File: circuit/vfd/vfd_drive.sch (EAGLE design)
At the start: 51 parts, among them J1 ZX62R-AB-5P, J2 DC_JACK_2DC0005D100, J8 FSM-21045-8, Q1 FA-238V, SW1 SKRPACE010, SW2 SKRPACE010, U1 PIC18F14K50-I, U2 MAX6921AWI+, U3 NJW4131, U4 DS3231M, U5 ADP3338AKCZ-3.3, U6 PSF-A85, U9 BME280

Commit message: [add]add all
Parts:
- removed J8: FSM-21045-8, taki-library:FSM-21045-8
- removed Q1: FA-238V, taki-library:FA-238V
- added C12: 0.1uF, taki-library:C-EUC0603
- added C17: 47pF, taki-library:C-EUC0603
- added J3: FSM-21045-10, taki-library:FSM-21045-10
- added J5: PSM-210223-10, taki-library:PSM-210223-10
- added LED1: RX, taki-library:LEDCHIPLED_0603
- added LED2: TX, taki-library:LEDCHIPLED_0603
- added LED4: VBUS, taki-library:LEDCHIPLED_0603
- added Q2, Q3: MMSS8050-L, taki-library:MMSS8050-L
- added R12, R13, R14: 1k, taki-library:R-EU_R0603
- added R15: 4.7k, taki-library:R-EU_R0603
- added R16, R19, R22, R23, R24: 10k, taki-library:R-EU_R0603
- added R17, R18: 27, taki-library:R-EU_R0603
- C16: value 0.1uF -> 47pF
- C3, C4: value 15pF -> 1uF
- J2: value DC_JACK_2DC0005D100 -> 2DC-0415D200; device taki-library:DC_JACK_2DC0005D100 -> taki-library:2DC-0415D200
- U1: value PIC18F14K50-I -> FT231XS; device taki-library:PIC18F14K50-I -> taki-library:FT231XS
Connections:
- removed net D_N: J1.D-, U1.RA1/D-
- removed net D_P: J1.D+, U1.RA0/D+
- removed net EN: C7.1, R3.1, R4.2
- removed net N$39: U1.VUSB
- removed net N$44: C3.1, Q1.1, U1.RA5/OSC1
- removed net N$45: C4.1, Q1.3, U1.RA4/OSC2
- removed net VBIAS: C1.1, DIS1.VBIAS
- new net D2_N: R17.2, U1.USBDM
- new net D2_P: R18.2, U1.USBDP
- new net DTR: Q3.E, R19.2, U1.!DTR
- new net D_N1: C16.1, J1.D-, R17.1
- new net D_P1: C17.1, J1.D+, R18.1
- new net N$14: R15.1, R16.2, U1.CBUS0
- new net N$15: Q2.B, R19.1
- new net N$16: Q3.B, R22.1
- new net N$17: R10.2
- new net N$18: J5.6, U2.VFBLANK
- new net N$19: R23.2, U6.GPIO15
- new net N$21: R24.1, U6.EN
- new net N$7: LED1.C, U1.CBUS1
- new net RESET: C7.1, Q2.C, R3.1, R4.2
- new net RTS: Q2.E, R22.2, U1.!RTS
- new net RXD: U1.RXD, U6.TX
- new net TXD: U1.TXD, U6.RX
- net +3V3: now also C12.1, C4.1, R12.2, R13.2, R24.2, U1.!RESET, U1.3V3OUT, U1.VCC, U1.VCCIO, U6.3V3; no longer C16.1, U1.VDD
- net +5V: now also C1.1, C3.1, DIS1.VBIAS, J5.1
- net GND: now also C12.2, C17.2, LED4.C, R16.1, R23.1, U1.GND@16, U1.GND@6, U2.GND, U6.GND1, U6.GND2; no longer Q1.2, Q1.4, U1.VSS
- net IO0: now also Q3.C
- net N$10: now also LED2.A, R13.1; no longer J8.5, U1.RC6/AN8
- net N$11: now also LED4.A, R14.1; no longer J8.4, U1.RC7/AN9
- net N$2: now also J5.2
- net N$3: now also J5.3
- net N$4: now also J5.4
- net N$5: now also J5.5
- net N$8: now also LED2.C, U1.CBUS2; no longer J8.7, U1.RC4/P1B
- net N$9: now also LED1.A, R12.1; no longer J8.6, U1.RC3/AN7
- net SCL: no longer U1.RB6
- net SDA: no longer U1.RB4/AN10
- net VBUS: now also R14.2, R15.2; no longer R10.2
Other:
- moved on the sheet: C15, C16, C3, C4, J1, J2

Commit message: [update]update from thinkpad
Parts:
- removed LED3: VBUS, taki-library:LEDCHIPLED_0603
- removed R10: 1k, taki-library:R-EU_R0603
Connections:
- removed net N$13: LED3.A, R10.1
- removed net N$17: R10.2
- net GND: no longer LED3.C
- net IO0: now also U6.GPIO0
- net RESET: now also U6.RESET
- net SDA: now also U6.GPIO14, U6.GPIO2
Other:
- moved on the sheet: R24
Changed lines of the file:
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@@
 </classes>
 <parts>
-<part name="SUPPLY1" library="taki-library" deviceset="GND" device=""/>
 <part name="R3" library="taki-library" deviceset="R-EU_" device="R0603" value="10k"/>
 <part name="C7" library="taki-library" deviceset="C-EU" device="C0603" value="1000pF "/>
@@
 <part name="GND8" library="taki-library" deviceset="GND" device=""/>
 <part name="+3V9" library="taki-library" deviceset="+3V3" device=""/>
-<part name="R10" library="taki-library" deviceset="R-EU_" device="R0603" value="1k"/>
-<part name="SUPPLY10" library="taki-library" deviceset="GND" device=""/>
 <part name="J1" library="taki-library" deviceset="ZX62" device="" technology="R-AB-5P"/>
-<part name="LED3" library="taki-library" deviceset="LED" device="CHIPLED_0603" value="VBUS"/>
 <part name="SW1" library="taki-library" deviceset="SKRPACE010" device=""/>
 <part name="SW2" library="taki-library" deviceset="SKRPACE010" device=""/>
@@
 </plain>
 <instances>
-<instance part="SUPPLY1" gate="GND" x="-154.94" y="88.9" smashed="yes">
-<attribute name="VALUE" x="-156.845" y="85.725" size="1.778" layer="96"/>
-</instance>
 <instance part="R3" gate="G$1" x="-116.84" y="-5.08" smashed="yes" rot="R90">
 <attribute name="NAME" x="-118.3386" y="-8.89" size="1.778" layer="95" rot="R90"/>
@@
 <attribute name="VALUE" x="-119.38" y="-40.64" size="1.778" layer="96" rot="R90"/>
 </instance>
-<instance part="R10" gate="G$1" x="-147.32" y="93.98" smashed="yes" rot="R90">
-<attribute name="NAME" x="-148.8186" y="90.17" size="1.778" layer="95" rot="R90"/>
-<attribute name="VALUE" x="-144.018" y="90.17" size="1.778" layer="96" rot="R90"/>
-</instance>
-<instance part="SUPPLY10" gate="GND" x="-147.32" y="73.66" smashed="yes">
-<attribute name="VALUE" x="-149.225" y="70.485" size="1.778" layer="96"/>
-</instance>
 <instance part="J1" gate="G$1" x="-266.7" y="-215.9" smashed="yes">
 <attribute name="NAME" x="-275.844" y="-207.772" size="1.778" layer="95"/>
 <attribute name="VALUE" x="-275.59" y="-231.14" size="1.778" layer="96"/>
 </instance>
-<instance part="LED3" gate="G$1" x="-147.32" y="83.82" smashed="yes">
-<attribute name="NAME" x="-143.764" y="79.248" size="1.778" layer="95" rot="R90"/>
-<attribute name="VALUE" x="-141.605" y="79.248" size="1.778" layer="96" rot="R90"/>
-</instance>
 <instance part="SW1" gate="G$1" x="-142.24" y="-12.7" smashed="yes" rot="R270">
 <attribute name="NAME" x="-144.78" y="-6.35" size="1.778" layer="95"/>
@@
 <attribute name="VALUE" x="-207.645" y="-3.175" size="1.778" layer="96"/>
 </instance>
-<instance part="R24" gate="G$1" x="-271.78" y="17.78" smashed="yes" rot="R90">
-<attribute name="NAME" x="-273.2786" y="13.97" size="1.778" layer="95" rot="R90"/>
-<attribute name="VALUE" x="-268.478" y="13.97" size="1.778" layer="96" rot="R90"/>
-</instance>
-<instance part="+3V5" gate="G$1" x="-271.78" y="27.94" smashed="yes">
-<attribute name="VALUE" x="-274.32" y="22.86" size="1.778" layer="96" rot="R90"/>
+<instance part="R24" gate="G$1" x="-271.78" y="22.86" smashed="yes" rot="R90">
+<attribute name="NAME" x="-273.2786" y="19.05" size="1.778" layer="95" rot="R90"/>
+<attribute name="VALUE" x="-268.478" y="19.05" size="1.778" layer="96" rot="R90"/>
+</instance>
+<instance part="+3V5" gate="G$1" x="-271.78" y="33.02" smashed="yes">
+<attribute name="VALUE" x="-274.32" y="27.94" size="1.778" layer="96" rot="R90"/>
 </instance>
 <instance part="+3V6" gate="G$1" x="-185.42" y="22.86" smashed="yes">
@@
 </net>
 <net name="GND" class="0">
-<segment>
-<pinref part="SUPPLY1" gate="GND" pin="GND"/>
-<wire x1="-154.94" y1="101.6" x2="-154.94" y2="91.44" width="0.1524" layer="91"/>
-</segment>
 <segment>
 <pinref part="J1" gate="G$1" pin="GND"/>
@@
 <pinref part="SW2" gate="G$1" pin="P"/>
 <pinref part="SW2" gate="G$1" pin="P1"/>
-</segment>
-<segment>
-<wire x1="-147.32" y1="78.74" x2="-147.32" y2="76.2" width="0.1524" layer="91"/>
-<pinref part="SUPPLY10" gate="GND" pin="GND"/>
-<pinref part="LED3" gate="G$1" pin="C"/>
 </segment>
 <segment>
@@
 <pinref part="R24" gate="G$1" pin="2"/>
 <pinref part="+3V5" gate="G$1" pin="+3V3"/>
-<wire x1="-271.78" y1="22.86" x2="-271.78" y2="25.4" width="0.1524" layer="91"/>
+<wire x1="-271.78" y1="27.94" x2="-271.78" y2="30.48" width="0.1524" layer="91"/>
 </segment>
 <segment>
@@
 <pinref part="Q2" gate="G$1" pin="C"/>
 </segment>
+<segment>
+<wire x1="-215.9" y1="15.24" x2="-205.74" y2="15.24" width="0.1524" layer="91"/>
+<pinref part="U6" gate="G$1" pin="RESET"/>
+<label x="-208.28" y="15.24" size="1.778" layer="95"/>
+</segment>
 </net>
 <net name="IO0" class="0">
@@
 <wire x1="-218.44" y1="-307.34" x2="-215.9" y2="-307.34" width="0.1524" layer="91"/>
 <pinref part="Q3" gate="G$1" pin="C"/>
+</segment>
+<segment>
+<wire x1="-246.38" y1="-25.4" x2="-246.38" y2="-17.78" width="0.1524" layer="91"/>
+<pinref part="U6" gate="G$1" pin="GPIO0"/>
+<label x="-246.38" y="-25.4" size="1.778" layer="95" rot="R90"/>
 </segment>
 </net>
@@
 </segment>
 </net>
-<net name="N$13" class="0">
-<segment>
-<pinref part="R10" gate="G$1" pin="1"/>
-<wire x1="-147.32" y1="86.36" x2="-147.32" y2="88.9" width="0.1524" layer="91"/>
-<pinref part="LED3" gate="G$1" pin="A"/>
-</segment>
-</net>
 <net name="VBATT" class="0">
 <segment>
@@
 <wire x1="-58.42" y1="45.72" x2="-58.42" y2="50.8" width="0.1524" layer="91"/>
 <junction x="-58.42" y="45.72"/>
+</segment>
+<segment>
+<pinref part="U6" gate="G$1" pin="GPIO2"/>
+<wire x1="-248.92" y1="-17.78" x2="-248.92" y2="-25.4" width="0.1524" layer="91"/>
+<label x="-248.92" y="-25.4" size="1.778" layer="95" rot="R90"/>
+</segment>
+<segment>
+<pinref part="U6" gate="G$1" pin="GPIO14"/>
+<wire x1="-264.16" y1="5.08" x2="-271.78" y2="5.08" width="0.1524" layer="91"/>
+<label x="-271.78" y="5.08" size="1.778" layer="95"/>
 </segment>
 </net>
@@
 <junction x="-220.98" y="-213.36"/>
 <pinref part="J1" gate="G$1" pin="D-"/>
-<label x="-154.94" y="109.22" size="1.778" layer="95"/>
 </segment>
 </net>
@@
 <junction x="-228.6" y="-215.9"/>
 <pinref part="J1" gate="G$1" pin="D+"/>
-<label x="-154.94" y="106.68" size="1.778" layer="95"/>
 </segment>
 </net>
@@
 </segment>
 </net>
-<net name="N$17" class="0">
-<segment>
-<pinref part="R10" gate="G$1" pin="2"/>
-<wire x1="-147.32" y1="99.06" x2="-147.32" y2="111.76" width="0.1524" layer="91"/>
-<wire x1="-147.32" y1="111.76" x2="-139.7" y2="111.76" width="0.1524" layer="91"/>
-<label x="-144.78" y="111.76" size="1.778" layer="95"/>
-</segment>
-</net>
 <net name="N$19" class="0">
 <segment>
@@
 <wire x1="-264.16" y1="10.16" x2="-271.78" y2="10.16" width="0.1524" layer="91"/>
 <pinref part="R24" gate="G$1" pin="1"/>
-<wire x1="-271.78" y1="10.16" x2="-271.78" y2="12.7" width="0.1524" layer="91"/>
-</segment>
-</net>
+<wire x1="-271.78" y1="10.16" x2="-271.78" y2="17.78" width="0.1524" layer="91"/>
+</segment>
+</net>

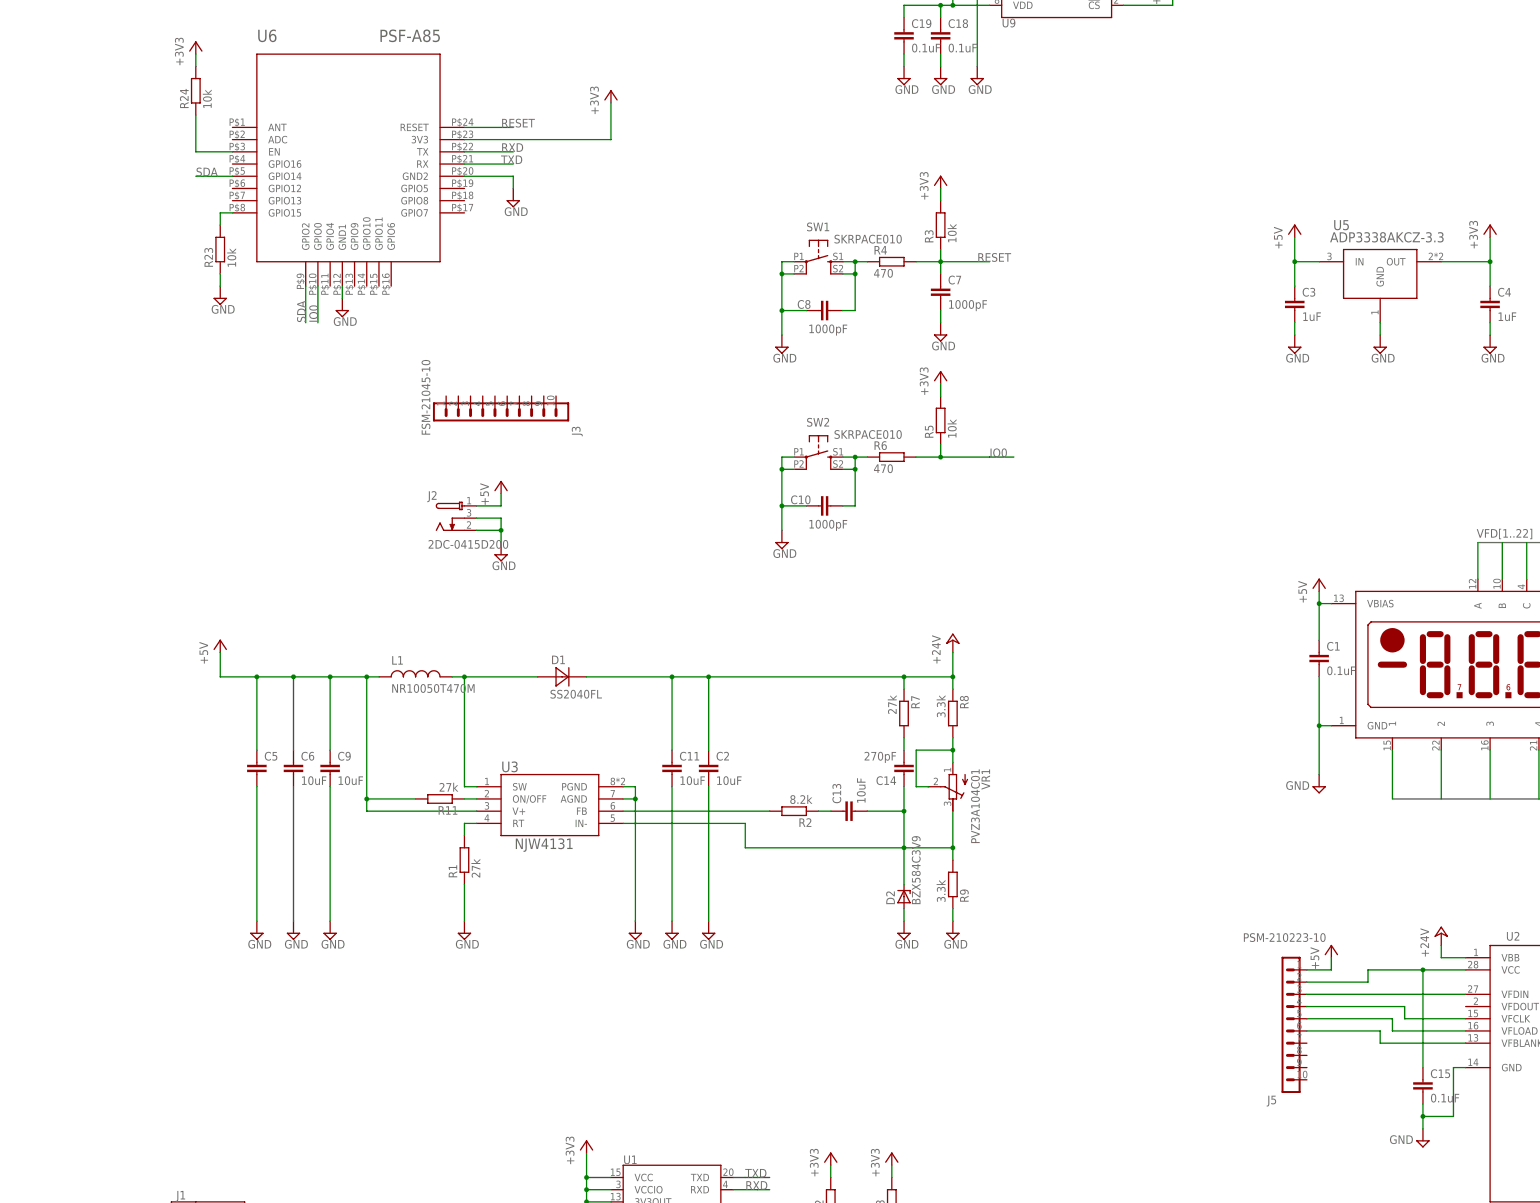
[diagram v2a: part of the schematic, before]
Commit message: [update]update connector routing
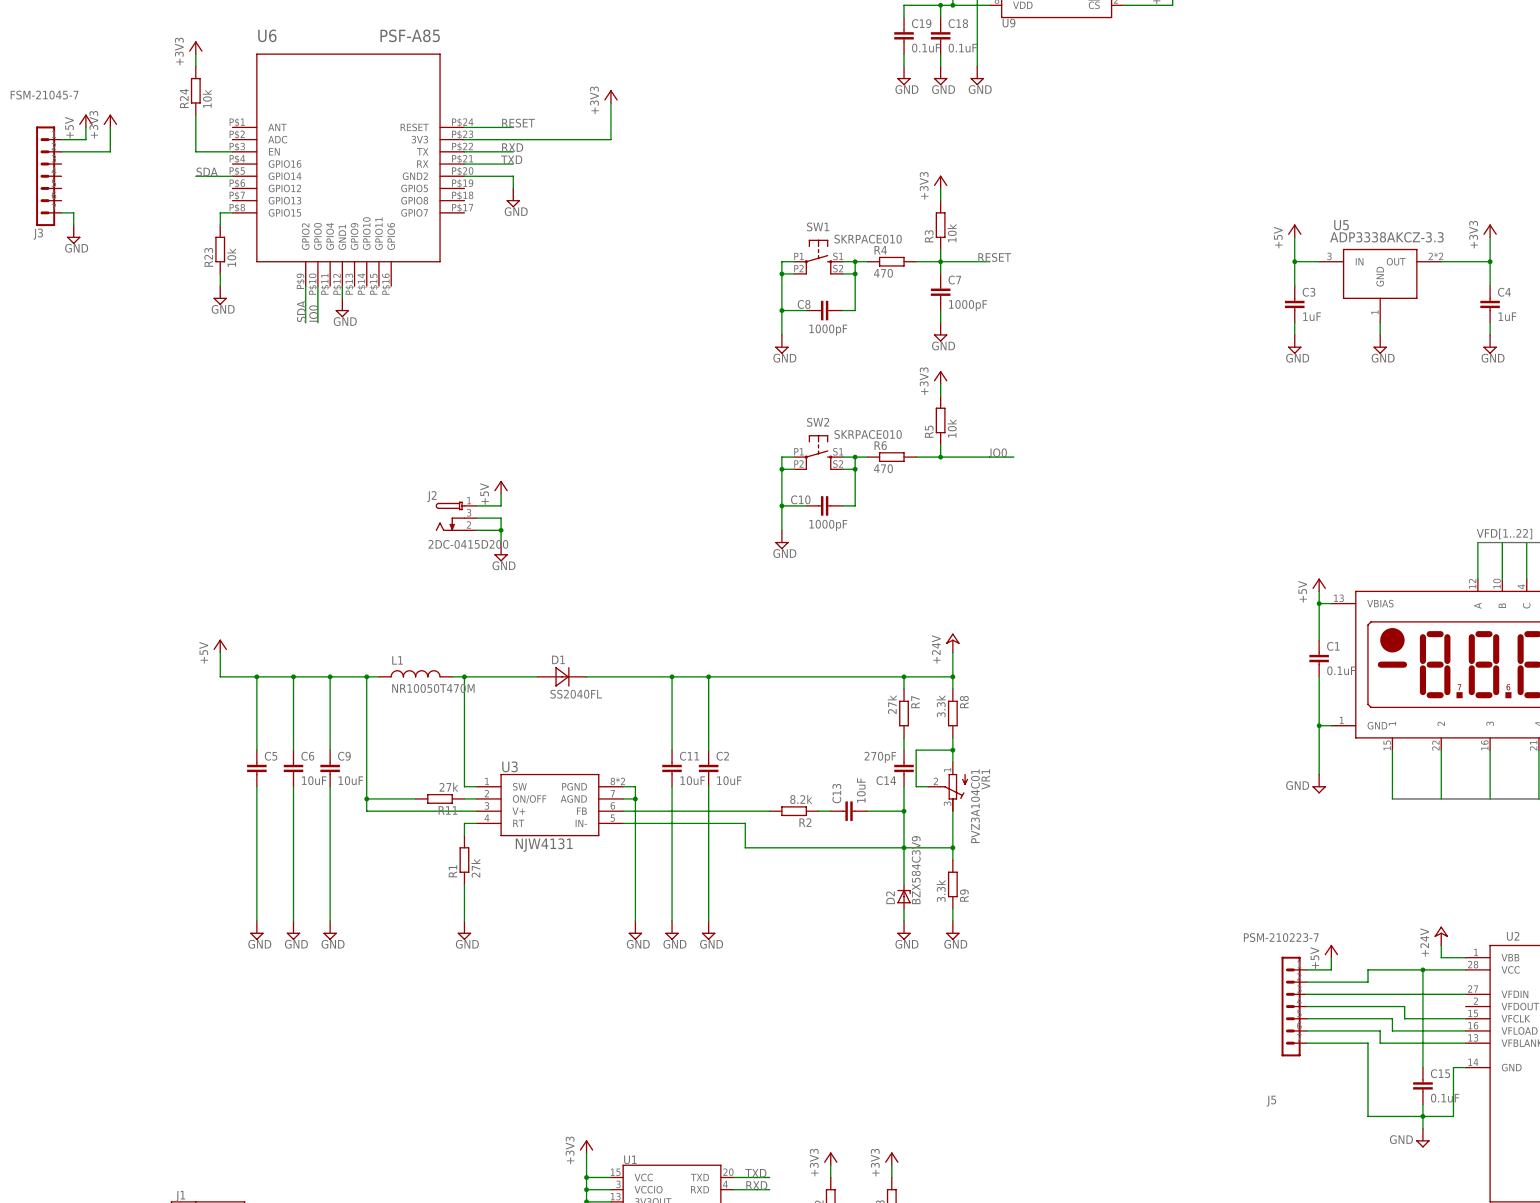
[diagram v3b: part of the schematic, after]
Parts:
- J3: value FSM-21045-10 -> FSM-21045-7; device taki-library:FSM-21045-10 -> taki-library:FSM-21045-7
- J5: value PSM-210223-10 -> PSM-210223-7; device taki-library:PSM-210223-10 -> taki-library:PSM-210223-7
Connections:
- net +3V3: now also J3.2
- net +5V: now also J3.1
- net GND: now also J3.7, J5.7
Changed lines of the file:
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@@
 <part name="SUPPLY2" library="taki-library" deviceset="GND" device=""/>
 <part name="J2" library="taki-library" deviceset="2DC-0415D200" device=""/>
-<part name="J3" library="taki-library" deviceset="FSM-21045-10" device=""/>
+<part name="J3" library="taki-library" deviceset="FSM-21045-7" device=""/>
 <part name="C3" library="taki-library" deviceset="C-EU" device="C0603" value="1uF"/>
 <part name="C4" library="taki-library" deviceset="C-EU" device="C0603" value="1uF"/>
@@
 <part name="Q2" library="taki-library" deviceset="MMSS8050" device="" technology="-L"/>
 <part name="Q3" library="taki-library" deviceset="MMSS8050" device="" technology="-L"/>
-<part name="J5" library="taki-library" deviceset="PSM-210223-10" device=""/>
+<part name="J5" library="taki-library" deviceset="PSM-210223-7" device=""/>
 <part name="P+2" library="taki-library" deviceset="+5V" device=""/>
 <part name="P+4" library="taki-library" deviceset="+5V" device=""/>
@@
 <part name="+3V5" library="taki-library" deviceset="+3V3" device=""/>
 <part name="+3V6" library="taki-library" deviceset="+3V3" device=""/>
+<part name="P+8" library="taki-library" deviceset="+5V" device=""/>
+<part name="+3V7" library="taki-library" deviceset="+3V3" device=""/>
+<part name="SUPPLY1" library="taki-library" deviceset="GND" device=""/>
 </parts>
 <sheets>
@@
 <attribute name="VALUE" x="-223.52" y="-72.39" size="1.778" layer="96"/>
 </instance>
-<instance part="J3" gate="G$1" x="-208.28" y="-45.72" smashed="yes">
-<attribute name="VALUE" x="-224.79" y="-48.895" size="1.778" layer="96" rot="MR90"/>
-<attribute name="NAME" x="-193.548" y="-48.895" size="1.778" layer="95" rot="MR90"/>
+<instance part="J3" gate="G$1" x="-304.8" y="1.27" smashed="yes" rot="R270">
+<attribute name="VALUE" x="-310.515" y="22.86" size="1.778" layer="96" rot="MR180"/>
+<attribute name="NAME" x="-305.435" y="-5.842" size="1.778" layer="95" rot="MR180"/>
 </instance>
 <instance part="C3" gate="G$1" x="-43.18" y="-20.32" smashed="yes">
@@
 <instance part="+3V6" gate="G$1" x="-185.42" y="22.86" smashed="yes">
 <attribute name="VALUE" x="-187.96" y="17.78" size="1.778" layer="96" rot="R90"/>
+</instance>
+<instance part="P+8" gate="1" x="-294.64" y="17.78" smashed="yes">
+<attribute name="VALUE" x="-297.18" y="12.7" size="1.778" layer="96" rot="R90"/>
+</instance>
+<instance part="+3V7" gate="G$1" x="-289.56" y="17.78" smashed="yes">
+<attribute name="VALUE" x="-292.1" y="12.7" size="1.778" layer="96" rot="R90"/>
+</instance>
+<instance part="SUPPLY1" gate="GND" x="-297.18" y="-7.62" smashed="yes">
+<attribute name="VALUE" x="-299.085" y="-10.795" size="1.778" layer="96"/>
 </instance>
 </instances>
@@
 <wire x1="-16.51" y1="-193.04" x2="-16.51" y2="-190.5" width="0.1524" layer="91"/>
 <wire x1="-16.51" y1="-190.5" x2="-16.51" y2="-187.96" width="0.1524" layer="91"/>
-<wire x1="-16.51" y1="-190.5" x2="-10.16" y2="-190.5" width="0.1524" layer="91"/>
+<wire x1="-16.51" y1="-190.5" x2="-15.24" y2="-190.5" width="0.1524" layer="91"/>
+<wire x1="-15.24" y1="-190.5" x2="-10.16" y2="-190.5" width="0.1524" layer="91"/>
 <wire x1="-10.16" y1="-190.5" x2="-10.16" y2="-180.34" width="0.1524" layer="91"/>
 <junction x="-16.51" y="-190.5"/>
 <pinref part="U2" gate="G$1" pin="GND"/>
 <wire x1="-10.16" y1="-180.34" x2="-7.62" y2="-180.34" width="0.1524" layer="91"/>
+<pinref part="J5" gate="G$1" pin="7"/>
+<wire x1="-40.64" y1="-175.26" x2="-27.94" y2="-175.26" width="0.1524" layer="91"/>
+<wire x1="-27.94" y1="-175.26" x2="-27.94" y2="-190.5" width="0.1524" layer="91"/>
+<wire x1="-27.94" y1="-190.5" x2="-16.51" y2="-190.5" width="0.1524" layer="91"/>
 </segment>
 <segment>
@@
 <pinref part="SUPPLY33" gate="GND" pin="GND"/>
 <wire x1="-205.74" y1="5.08" x2="-205.74" y2="2.54" width="0.1524" layer="91"/>
+</segment>
+<segment>
+<pinref part="J3" gate="G$1" pin="7"/>
+<wire x1="-299.72" y1="-2.54" x2="-297.18" y2="-2.54" width="0.1524" layer="91"/>
+<pinref part="SUPPLY1" gate="GND" pin="GND"/>
+<wire x1="-297.18" y1="-2.54" x2="-297.18" y2="-5.08" width="0.1524" layer="91"/>
 </segment>
 </net>
@@
 <pinref part="+3V6" gate="G$1" pin="+3V3"/>
 <wire x1="-185.42" y1="12.7" x2="-185.42" y2="20.32" width="0.1524" layer="91"/>
+</segment>
+<segment>
+<pinref part="+3V7" gate="G$1" pin="+3V3"/>
+<wire x1="-289.56" y1="15.24" x2="-289.56" y2="10.16" width="0.1524" layer="91"/>
+<pinref part="J3" gate="G$1" pin="2"/>
+<wire x1="-289.56" y1="10.16" x2="-299.72" y2="10.16" width="0.1524" layer="91"/>
 </segment>
 </net>
@@
 <wire x1="-208.28" y1="-63.5" x2="-208.28" y2="-60.96" width="0.1524" layer="91"/>
 </segment>
+<segment>
+<pinref part="J3" gate="G$1" pin="1"/>
+<wire x1="-299.72" y1="12.7" x2="-294.64" y2="12.7" width="0.1524" layer="91"/>
+<pinref part="P+8" gate="1" pin="+5V"/>
+<wire x1="-294.64" y1="12.7" x2="-294.64" y2="15.24" width="0.1524" layer="91"/>
+</segment>
 </net>
